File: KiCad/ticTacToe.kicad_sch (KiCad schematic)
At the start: 30 parts, among them J1 Barrel_Jack_Switch, J2 Conn_01x02_Pin, J3 Conn_01x04_Pin, SW1 SPDT_RGB, SW10 SW_Push_LED, SW11 SW_Push_LED, SW12 SW_SPST, SW2 SPDT_RGB, SW3 SPDT_RGB, SW4 SPDT_RGB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

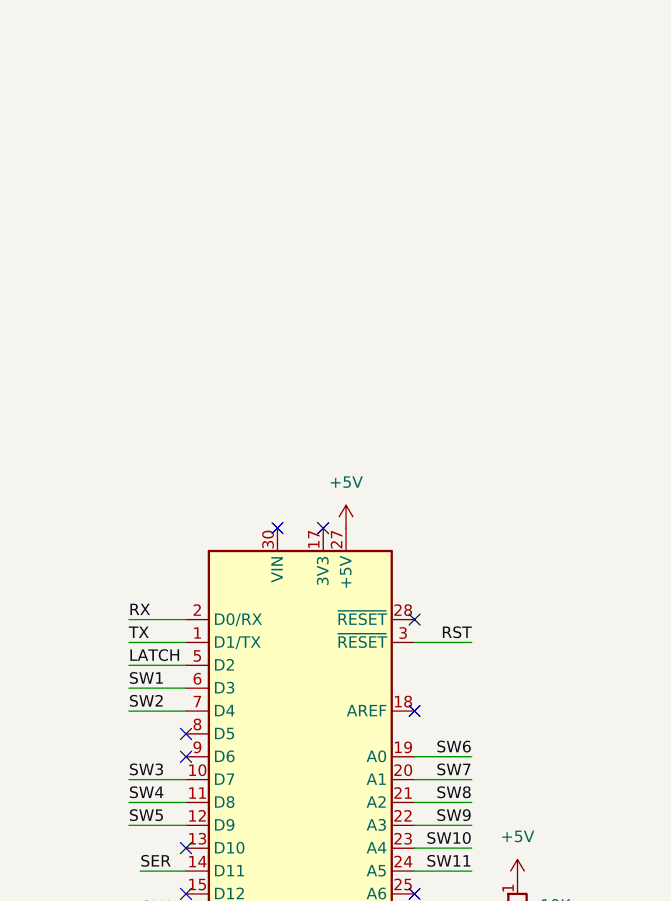
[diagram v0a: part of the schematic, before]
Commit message: Added speaker to the schematic
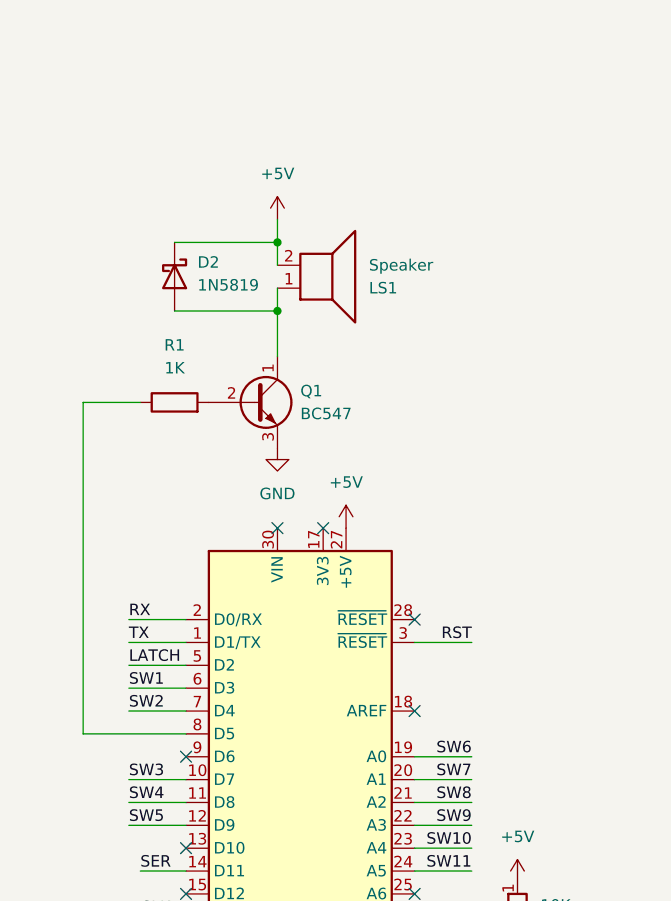
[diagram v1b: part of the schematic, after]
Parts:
- added D2: 1N5819, Diode_THT:D_DO-41_SOD81_P7.62mm_Horizontal, symbol Diode:1N5819
- added LS1: Speaker, Connector_PinHeader_2.54mm:PinHeader_1x02_P2.54mm_Vertical, symbol Device:Speaker
- added Q1: BC547, Package_TO_SOT_THT:TO-92_Inline_Wide, symbol Transistor_BJT:BC547
- added R1: 1K, Resistor_THT:R_Axial_DIN0204_L3.6mm_D1.6mm_P7.62mm_Horizontal, symbol Device:R
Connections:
- net +5V: now also D2.1 (K), LS1.2
- net GND: now also Q1.3 (E)
- net at A1.8 (D5): now also R1.1
- new net: D2.2 (A), LS1.1, Q1.1 (C)
- new net: Q1.2 (B), R1.2
- no-connect marks 23 -> 22
